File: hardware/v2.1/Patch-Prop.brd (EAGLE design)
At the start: 57 x 29 mm, 51 parts, among them IC2 ATMEGA168, IC3 MCP1253, IC5 MMA8452Q, IC6 W2RV005RM, IC7 MCP73831

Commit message: Switch for charging topology, added jumper for FTDI, Stepup to V+
-Added a header for a switch between battery and V+. When the switch is
off, only the charger IC is still connected to the battery
-Disconnected FTDI from +3v3 now jumper to V+
-Now connected setupup to V+ instead of +3v3
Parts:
- added SJ4: SOLDERJUMPERNO, SparkFun:SJ_2S-NO
- added SWITCH: (no value), SparkFun:1X02
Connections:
- new net N$13: FTDI.4, SJ4.1
- new net VBATT: BATT.2, C2.1, IC7.3, SWITCH.2
- net +3V3: no longer C8.1, FTDI.4, IC3.3, IC3.7
- net V+: now also C8.1, IC3.3, IC3.7, SJ4.2, SWITCH.1; no longer BATT.2, C2.1, IC7.3
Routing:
- net +3V3: track 144.7 -> 131.3 mm
- net V+: track 163.3 -> 168.5 mm

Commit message: Flipped transistor footprint
Flipped to the more common BCE/DGS layout
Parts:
- removed T1: (no value), transistor:SOT23-EBC
- added Q1: (no value), SparkFun:SOT23
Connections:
- net N$4: now also Q1.2; no longer T1.E
- net VIBE: now also Q1.3; no longer T1.C
- net VIBE_CONTROL: now also Q1.1; no longer T1.B
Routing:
- net N$4: track 2.87 -> 0.07 mm
- net VIBE_CONTROL: track 25.5 -> 24.5 mm
- net VIBE: track 7.16 -> 6.56 mm
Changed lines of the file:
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@@
 <attribute name="VALUE" x="46.651" y="25.908" size="0.6096" layer="28" font="vector" ratio="15" rot="MR270"/>
-</element>
-<element name="T1" library="transistor" package="SOT23-EBC" value="" x="20" y="26" smashed="yes" rot="MR180">
-<attribute name="NAME" x="21.905" y="25.395" size="1.016" layer="26" font="vector" ratio="20" rot="MR90"/>
-<attribute name="VALUE" x="18.095" y="29.175" size="1.27" layer="28" rot="MR180"/>
 </element>
 <element name="PWR" library="led" package="CHIPLED_0805" value="" x="5.8" y="18.5" smashed="yes">
@@
 <element name="SWITCH" library="SparkFun" package="1X02" value="" x="-5" y="-10"/>
 <element name="SJ4" library="SparkFun" package="SJ_2S-NO" value="SOLDERJUMPERNO" x="-10" y="-9"/>
+<element name="Q1" library="SparkFun" package="SOT23" value="" x="20" y="26" rot="MR180"/>
 </elements>
 <signals>
@@
 </signal>
 <signal name="VIBE_CONTROL">
-<contactref element="T1" pad="B"/>
 <via x="23.8" y="23.4" extent="1-16" drill="0.5" shape="octagon"/>
-<wire x1="20.95" y1="27.1" x2="21.9" y2="27.1" width="0.3048" layer="16"/>
 <wire x1="21.9" y1="27.1" x2="22.5" y2="26.5" width="0.3048" layer="16"/>
 <wire x1="22.5" y1="26.5" x2="22.5" y2="24.7" width="0.3048" layer="16"/>
@@
 <wire x1="36" y1="14.5" x2="29.9" y2="20.6" width="0.3048" layer="1"/>
 <wire x1="29.9" y1="20.6" x2="29.9" y2="22.9" width="0.3048" layer="1"/>
+<contactref element="Q1" pad="1"/>
+<wire x1="21.9" y1="27.1" x2="19.05" y2="27.1" width="0" layer="19" extent="16-16"/>
 </signal>
 <signal name="VIBE">
-<contactref element="T1" pad="C"/>
 <contactref element="VIBE" pad="2"/>
-<wire x1="20" y1="24.9" x2="20.6" y2="24.9" width="0.3048" layer="16"/>
 <wire x1="20.6" y1="24.9" x2="23.5" y2="22" width="0.3048" layer="16"/>
 <wire x1="23.5" y1="22" x2="25.96" y2="22" width="0.3048" layer="16"/>
+<contactref element="Q1" pad="3"/>
+<wire x1="20.6" y1="24.9" x2="20" y2="24.9" width="0" layer="19" extent="16-16"/>
 </signal>
 <signal name="USB_VIN">
@@
 </signal>
 <signal name="N$4">
-<contactref element="T1" pad="E"/>
 <contactref element="R1" pad="2"/>
-<wire x1="19.05" y1="27.1" x2="16.25" y2="27.1" width="0.3048" layer="16"/>
 <wire x1="16.25" y1="27.1" x2="16.2" y2="27.15" width="0.3048" layer="16"/>
+<contactref element="Q1" pad="2"/>
+<wire x1="16.25" y1="27.1" x2="20.95" y2="27.1" width="0" layer="19" extent="16-16"/>
 </signal>
 <signal name="N$7">

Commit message: Working on routing, noting progress
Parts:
- moved SJ4 54.3 mm to (36.3, 19.3), turned to 180 degrees
- moved C15 43.3 mm to (23.6, 30.9), flipped to the bottom, turned to 180 degrees
- moved SJ3 29.9 mm to (16.8, 15.3), flipped to the bottom, turned to 270 degrees
- moved IC4 25.2 mm to (18.9, 16.0), flipped to the bottom
- moved SWITCH 20.2 mm to (2.00, 9.00), turned to 90 degrees
- moved IO1 2.00 mm to (2.00, 15.0)
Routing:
- net GND: track 245.9 -> 229.6 mm
- net VBATT: track 0.34 -> 13.3 mm
- net +3V3: track 131.3 -> 120.4 mm
- net V+: track 168.5 -> 178.8 mm
- net N$4: track 0.07 -> 6.29 mm
- net N$13: track 0.00 -> 2.85 mm
- net GREEN_OUT: track 103.6 -> 101.5 mm
- net VIBE_CONTROL: track 24.5 -> 26.4 mm
- net N$2: track 0.00 -> 1.65 mm
- net DTR: track 4.06 -> 5.62 mm
- net RESET: track 46.1 -> 47.6 mm
- net ADC3: track 38.1 -> 39.5 mm
- net N$6: track 11.0 -> 12.4 mm
- net N$3: track 10.5 -> 11.7 mm
- net ADC2: track 36.8 -> 37.9 mm
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
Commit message: Routing away
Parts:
- moved C15 8.84 mm to (17.5, 24.5), turned to 90 degrees
- moved R1 0.80 mm to (15.4, 26.3)
- moved C13 0.50 mm to (20.9, 11.5)
- moved Q1 0.50 mm to (20.5, 26.0)
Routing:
- net +3V3: track 120.4 -> 142.2 mm, vias 4 -> 6
- net GND: track 229.6 -> 243.4 mm, vias 13 -> 15
- net N$1: track 0.00 -> 6.54 mm
- net V+: track 178.8 -> 182.0 mm, vias 10 -> 11
- net N$10: track 26.1 -> 27.4 mm
- net N$3: track 11.7 -> 12.7 mm
- net N$4: track 6.29 -> 7.02 mm
- net N$8: track 8.05 -> 7.35 mm
- net N$6: track 12.4 -> 13.0 mm
- net VIBE_CONTROL: track 26.4 -> 25.9 mm
- net VIBE: track 7.16 -> 6.66 mm

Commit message: Finished routing changes
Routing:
- net VBATT: track 13.3 -> 44.4 mm, vias 0 -> 4
- net USB_VIN: track 26.3 -> 32.6 mm
- net N$8: track 7.35 -> 5.20 mm
- net +3V3: track 142.2 -> 140.2 mm
- net V+: track 182.0 -> 182.8 mm
- net N$14: track 7.02 -> 7.68 mm

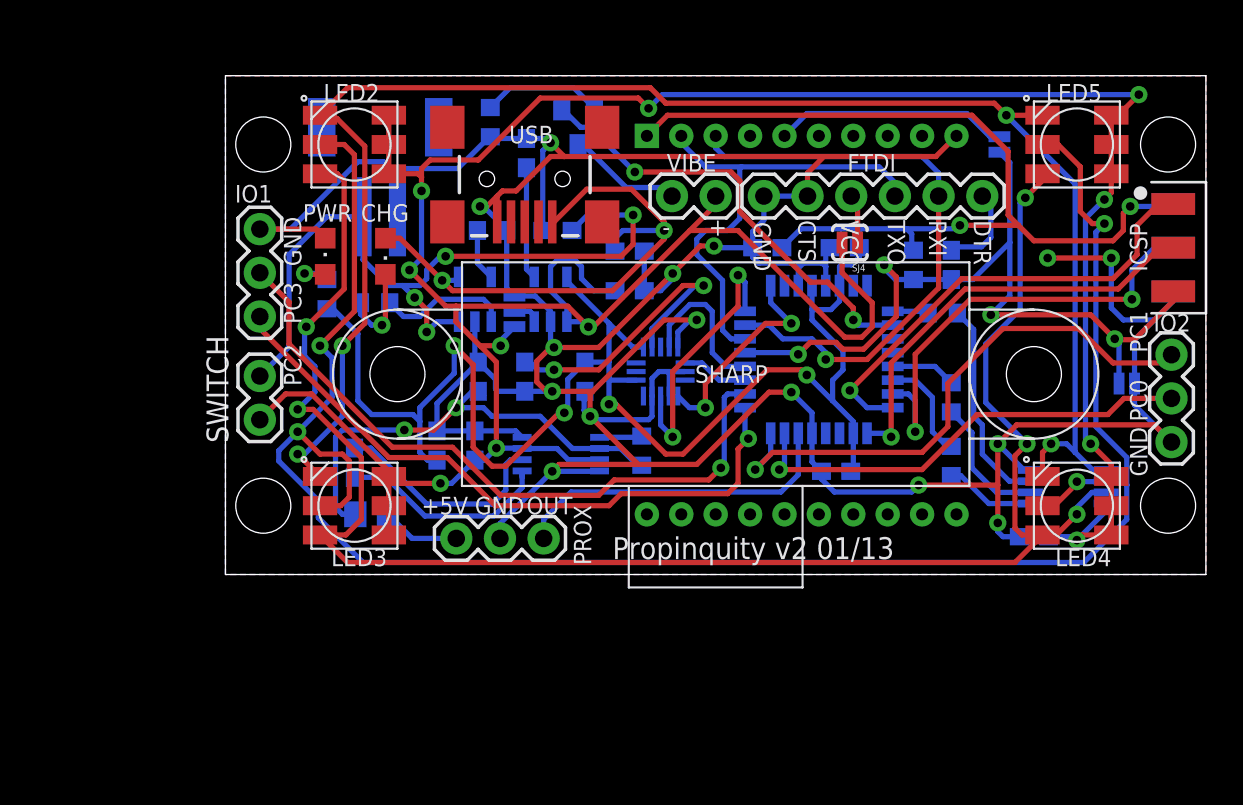
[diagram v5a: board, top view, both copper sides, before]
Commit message: Upped the DRC tolerance to 10mil where possible
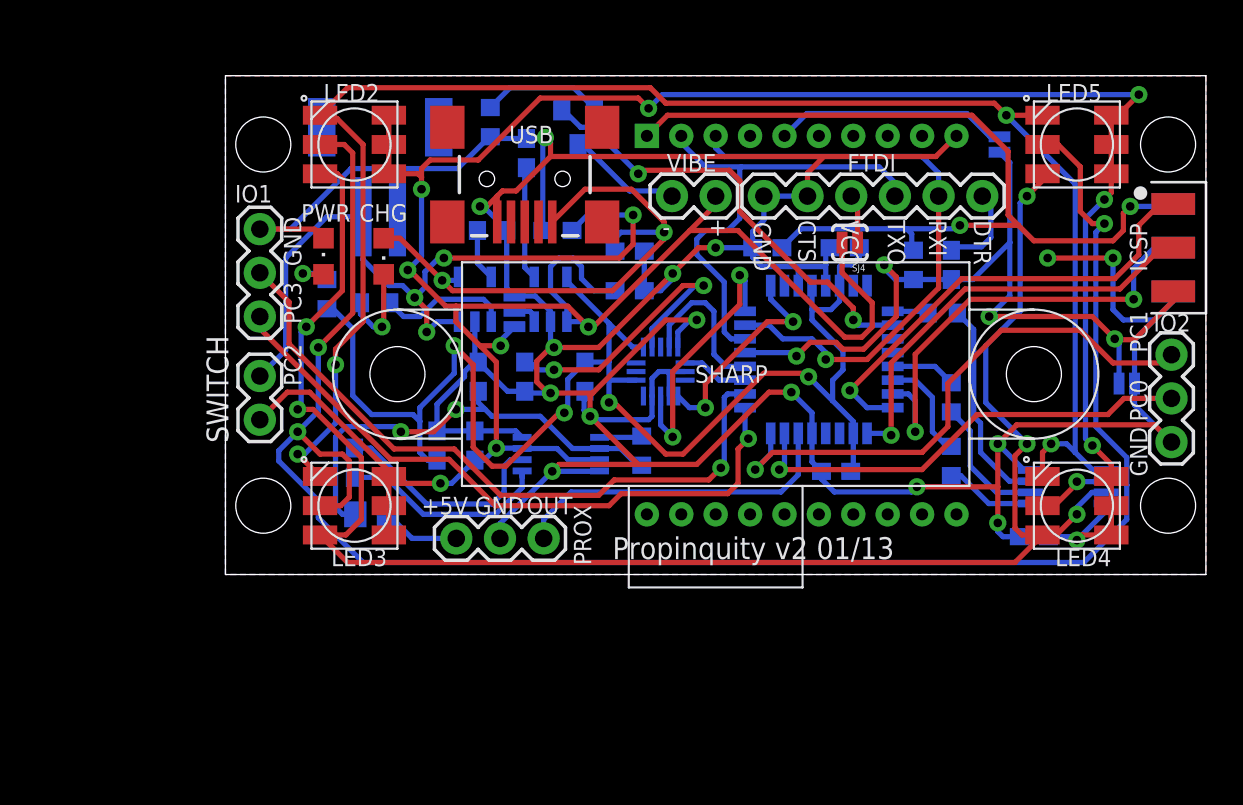
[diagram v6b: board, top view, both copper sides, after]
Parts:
- moved CHG 0.10 mm to (9.20, 18.5)
- moved PWR 0.10 mm to (5.70, 18.5)
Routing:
- net GND: track 243.4 -> 242.0 mm
- net RED_OUT: track 114.6 -> 113.9 mm
- net GREEN_OUT: track 101.3 -> 100.7 mm
